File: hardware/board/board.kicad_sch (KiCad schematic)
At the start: 1 part, among them U1 RP2040

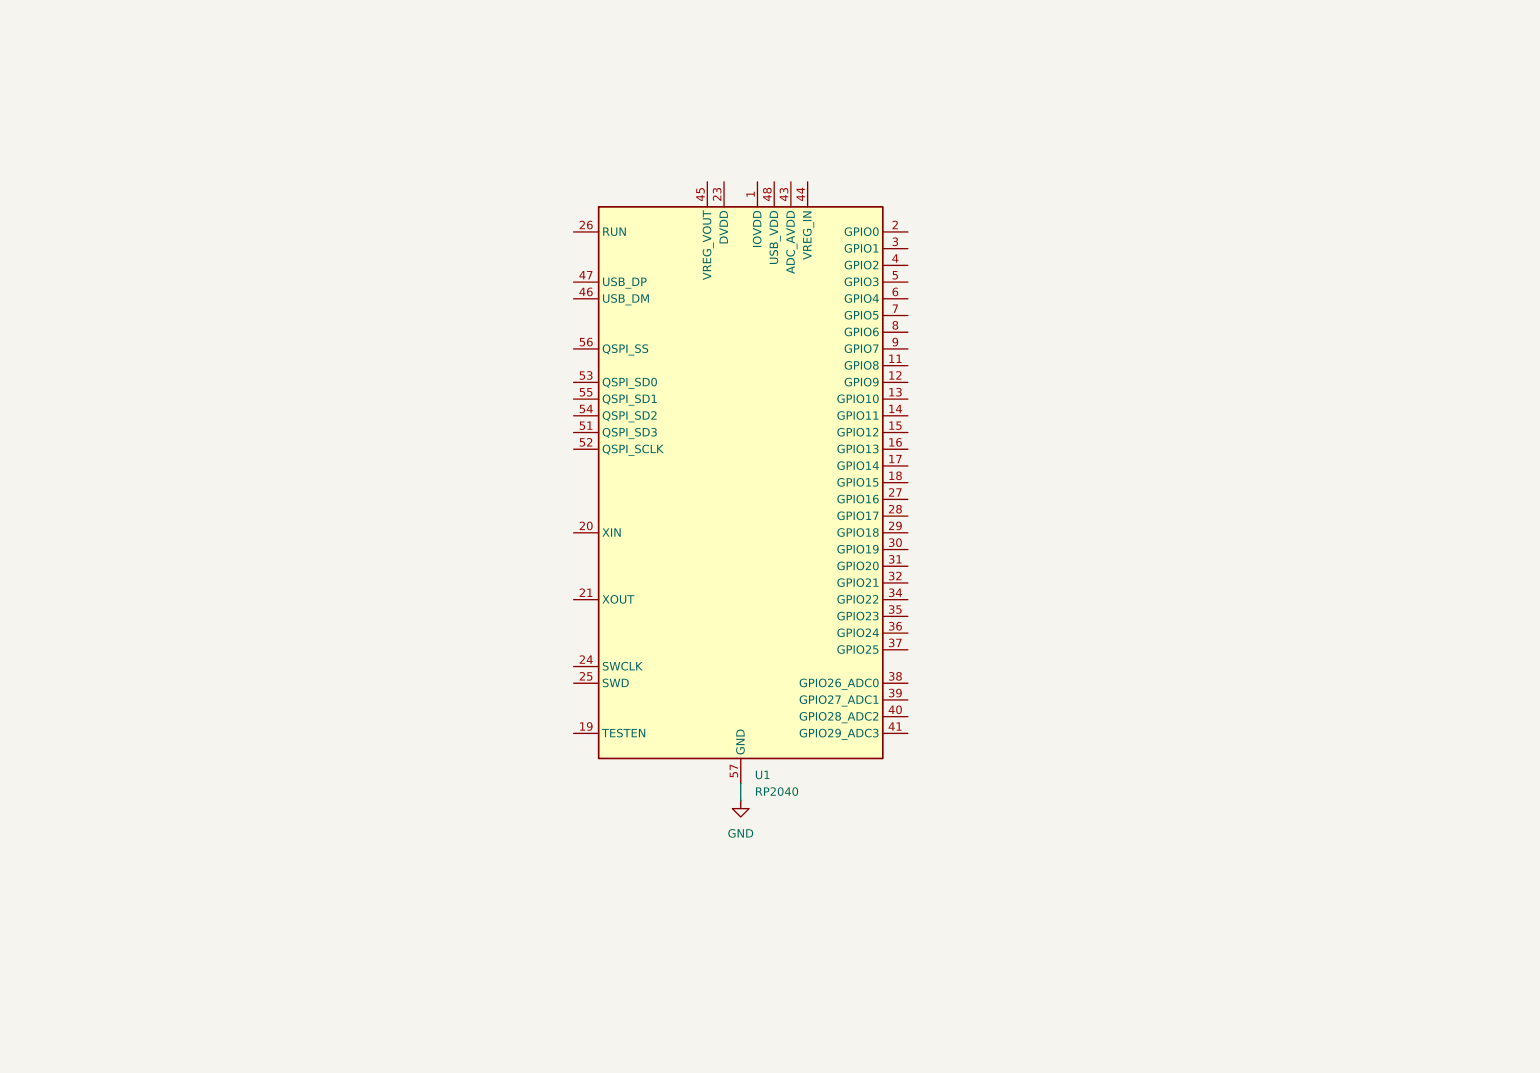
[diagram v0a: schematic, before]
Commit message: add hierarchical sheets
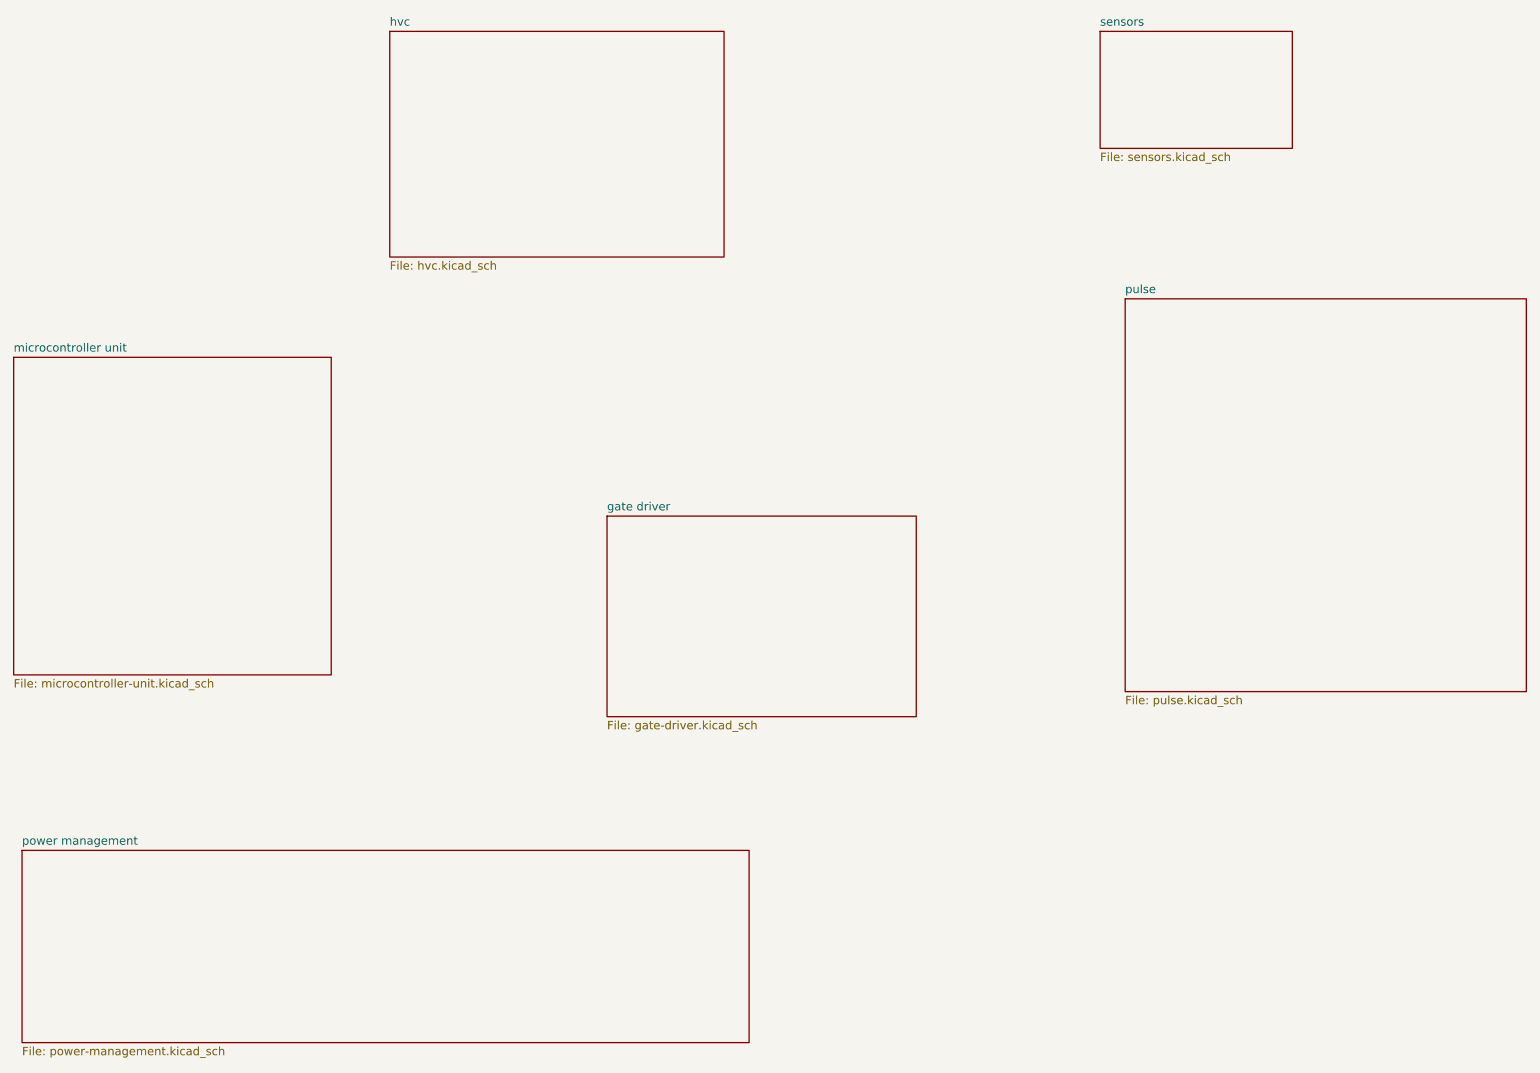
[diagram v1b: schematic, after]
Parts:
- removed U1: RP2040, Package_DFN_QFN:QFN-56-1EP_7x7mm_P0.4mm_EP3.2x3.2mm, symbol MCU_RaspberryPi:RP2040
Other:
- added sheet gate driver (gate-driver.kicad_sch)
- added sheet hvc (hvc.kicad_sch)
- added sheet microcontroller unit (microcontroller-unit.kicad_sch)
- added sheet power management (power-management.kicad_sch)
- added sheet pulse (pulse.kicad_sch)
- added sheet sensors (sensors.kicad_sch)
